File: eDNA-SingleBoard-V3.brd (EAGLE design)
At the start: 107 x 70 mm, 96 parts, among them J1 PJS008U-3000-0, J2 MEM2051-00-195-00-A, Q1 DMN65D8L-7, Q2 DMN65D8L-7, Q3 DMN65D8L-7, U1 TXS0108EPWR

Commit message: Update .brd
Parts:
- moved U$2 0.68 mm to (68.6, 65.5)
- moved C12 0.51 mm to (74.0, 59.7)
- moved R14 0.51 mm to (74.0, 55.0)
- moved J2 0.51 mm to (9.02, 35.6)
- moved DRV8871 0.51 mm to (68.6, 57.0)
- moved C18 0.25 mm to (24.4, 42.9)
- moved RTC 0.25 mm to (23.1, 35.6)
- moved C3 0.25 mm to (23.0, 28.2)
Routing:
- net +5V: track 179.2 -> 216.7 mm, vias 6 -> 10
- net DGND: track 5.39 -> 0.00 mm, vias 40 -> 41
- net SHUTDOWN: track 62.8 -> 66.1 mm
- net SCK: track 45.0 -> 44.5 mm
- net HB_IN2: track 72.4 -> 71.9 mm
- net HB_IN1: track 67.2 -> 66.7 mm

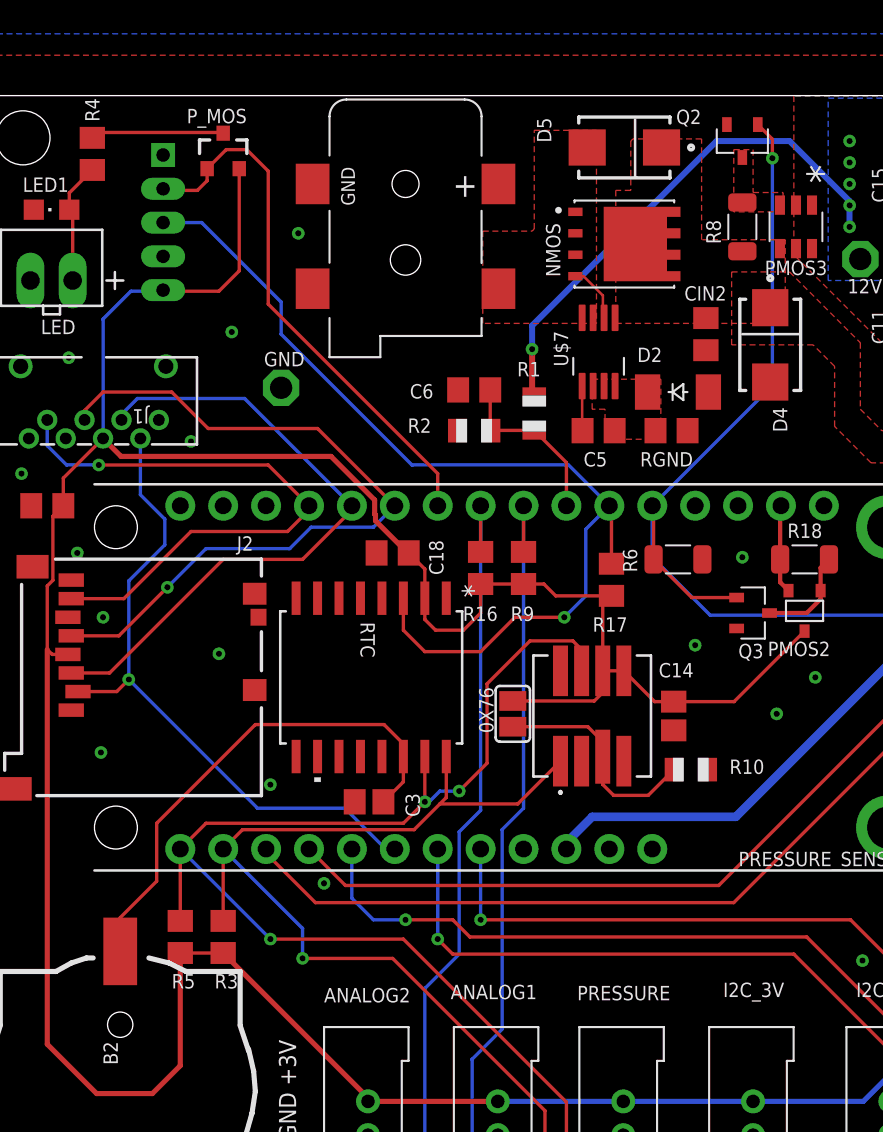
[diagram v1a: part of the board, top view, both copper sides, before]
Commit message: Added External Interrupt
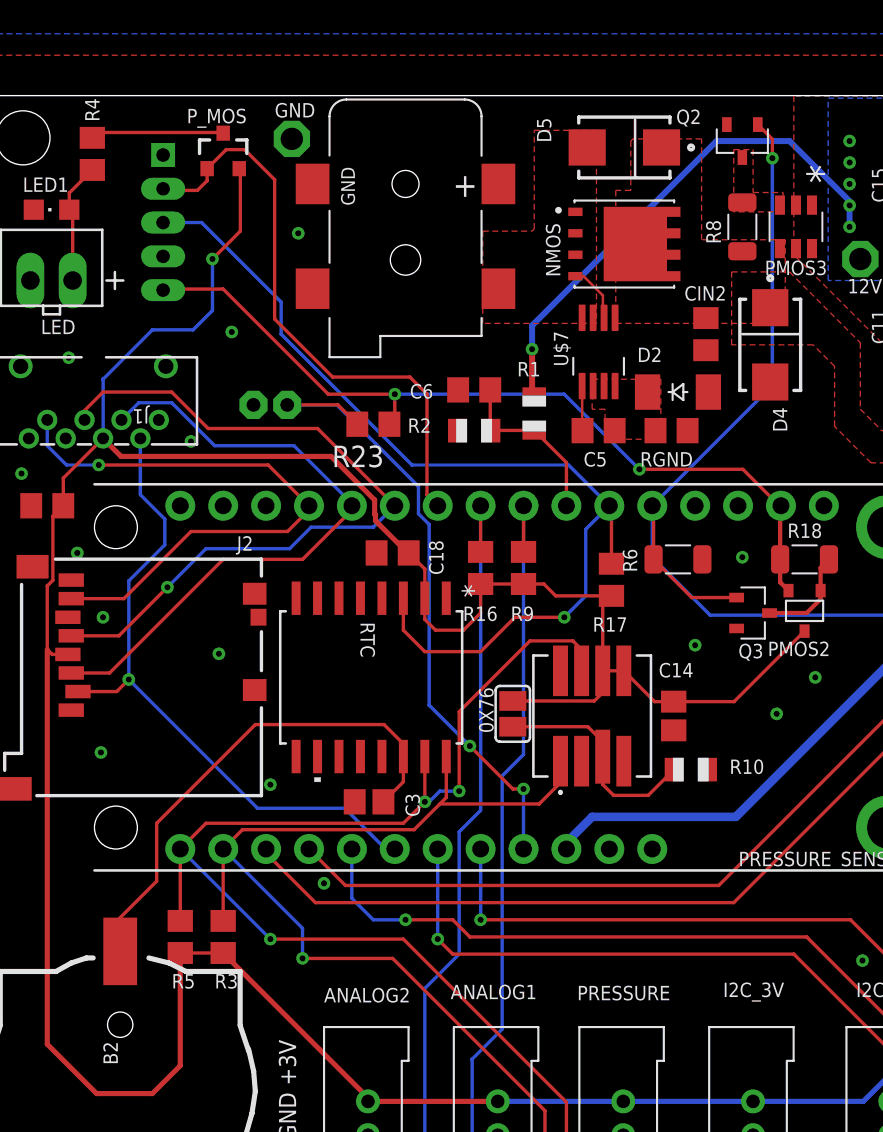
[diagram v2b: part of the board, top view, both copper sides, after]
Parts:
- added BUTTON: (no value), jst-ph:JST-PH2
- added R23: 10K, rcl:R0805
- moved GND 14.7 mm to (18.4, 67.4)
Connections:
- net +3V3: no longer SWITCH.5
- net 3V_MCU: now also R23.1, SWITCH.5
- net BUTTON1: now also BUTTON.2, R23.2
- net DGND: now also BUTTON.1
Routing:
- net 3V_MCU: track 5.25 -> 49.0 mm, vias 0 -> 2
- net BUTTON1: track 0.00 -> 38.8 mm, vias 0 -> 2
- net WAKE_NOSLEEP: track 32.2 -> 34.8 mm
- net +3V3: track 221.8 -> 220.2 mm, vias 1 -> 2
- net SCL: track 91.5 -> 92.3 mm
